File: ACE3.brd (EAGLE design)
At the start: 160 x 100 mm, 141 parts, among them IC1 7805T, IC2 74HCT04N, IC3 74HCT08N, Q1 2N3904, Q3 BC237, T1 2N2369, X1 6.556MHz

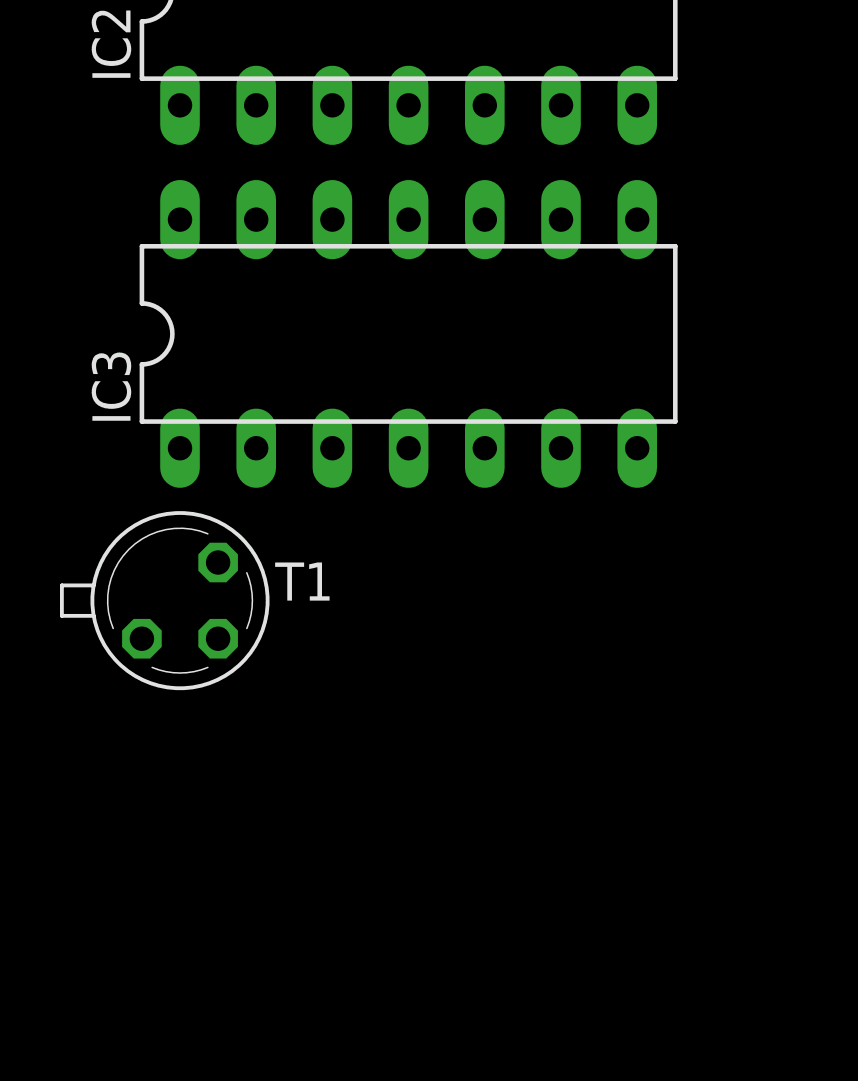
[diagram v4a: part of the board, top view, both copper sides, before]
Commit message: Make sure is correct this time. OR not AnD where needed.
Signed-off-by: John Bradley <flypie@rocketmail.com>
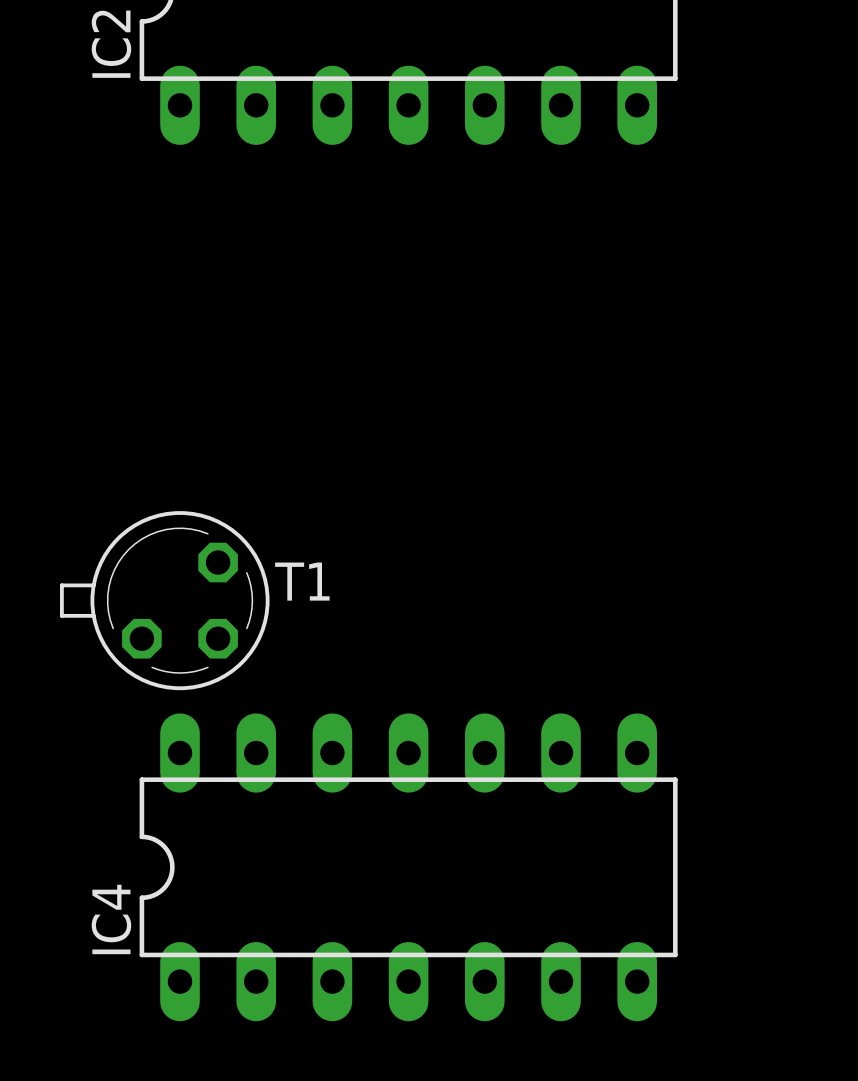
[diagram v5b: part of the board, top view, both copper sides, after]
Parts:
- removed IC3: 74HCT08N, 74xx-eu:DIL14
- added IC4: 74LS32N, 74xx-eu:DIL14
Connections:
- net ADDRESS12: now also IC4.1; no longer IC3.4
- net GND: now also IC4.7; no longer IC3.7
- net N$2: now also IC4.3; no longer IC3.3
- net N$30: now also IC4.4; no longer IC3.1
- net N$6: now also IC4.2, IC4.5; no longer IC3.2, IC3.5
- net N$7: now also IC4.6; no longer IC3.6
- net VCC: now also IC4.14; no longer IC3.14
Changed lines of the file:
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@@
 <attribute name="VALUE" x="-154.051" y="-6.985" size="1.27" layer="27" ratio="10"/>
-</element>
-<element name="IC3" library="74xx-eu" library_urn="urn:adsk.eagle:library:85" package="DIL14" package3d_urn="urn:adsk.eagle:package:16407/2" value="74HCT08N" x="-147.32" y="-17.78" smashed="yes">
-<attribute name="NAME" x="-156.591" y="-20.828" size="1.27" layer="25" ratio="10" rot="R90"/>
-<attribute name="VALUE" x="-154.051" y="-18.415" size="1.27" layer="27" ratio="10"/>
 </element>
 <element name="T1" library="transistor" library_urn="urn:adsk.eagle:library:402" package="TO18" package3d_urn="urn:adsk.eagle:package:28526/2" value="2N2369" x="-154.94" y="-26.67" smashed="yes">
 <attribute name="NAME" x="-151.765" y="-26.67" size="1.27" layer="25" ratio="10"/>
 <attribute name="VALUE" x="-151.765" y="-28.575" size="1.27" layer="27" ratio="10"/>
+</element>
+<element name="IC4" library="74xx-eu" library_urn="urn:adsk.eagle:library:85" package="DIL14" package3d_urn="urn:adsk.eagle:package:16407/2" value="74LS32N" x="-147.32" y="-35.56" smashed="yes">
+<attribute name="NAME" x="-156.591" y="-38.608" size="1.27" layer="25" ratio="10" rot="R90"/>
+<attribute name="VALUE" x="-154.051" y="-36.195" size="1.27" layer="27" ratio="10"/>
 </element>
 </elements>
@@
 <contactref element="Z1-2" pad="27"/>
 <contactref element="IC2" pad="14"/>
-<contactref element="IC3" pad="14"/>
-<wire x1="-154.94" y1="-2.54" x2="-154.94" y2="-13.97" width="0" layer="19" extent="1-1"/>
+<contactref element="IC4" pad="14"/>
+<wire x1="-154.94" y1="-2.54" x2="-154.94" y2="-31.75" width="0" layer="19" extent="1-1"/>
 <wire x1="-101.6" y1="2.54" x2="-154.94" y2="-2.54" width="0" layer="19" extent="1-1"/>
 <wire x1="-86.36" y1="2.54" x2="-101.6" y2="2.54" width="0" layer="19" extent="1-1"/>
@@
 <contactref element="Z5-6" pad="19"/>
 <contactref element="IC2" pad="7"/>
-<contactref element="IC3" pad="7"/>
 <contactref element="T1" pad="1"/>
-<wire x1="-139.7" y1="-21.59" x2="-156.21" y2="-27.94" width="0" layer="19" extent="1-1"/>
-<wire x1="-139.7" y1="-10.16" x2="-139.7" y2="-21.59" width="0" layer="19" extent="1-1"/>
+<contactref element="IC4" pad="7"/>
+<wire x1="-139.7" y1="-39.37" x2="-156.21" y2="-27.94" width="0" layer="19" extent="1-1"/>
+<wire x1="-139.7" y1="-10.16" x2="-156.21" y2="-27.94" width="0" layer="19" extent="1-1"/>
 <wire x1="-99.06" y1="17.78" x2="-139.7" y2="-10.16" width="0" layer="19" extent="1-1"/>
 <wire x1="-92.71" y1="33.02" x2="-99.06" y2="17.78" width="0" layer="19" extent="1-1"/>
@@
 <contactref element="Z3-4" pad="2"/>
 <contactref element="Z52" pad="2"/>
-<contactref element="IC3" pad="4"/>
+<contactref element="IC4" pad="1"/>
 <contactref element="IC2" pad="1"/>
-<wire x1="-154.94" y1="-10.16" x2="-147.32" y2="-21.59" width="0" layer="19" extent="1-1"/>
+<wire x1="-154.94" y1="-10.16" x2="-154.94" y2="-39.37" width="0" layer="19" extent="1-1"/>
 <wire x1="-124.46" y1="2.54" x2="-154.94" y2="-10.16" width="0" layer="19" extent="1-1"/>
 <wire x1="-123.19" y1="33.02" x2="-124.46" y2="2.54" width="0" layer="19" extent="1-1"/>
@@
 <contactref element="R26" pad="1"/>
 <contactref element="Z26" pad="2"/>
-<contactref element="IC3" pad="3"/>
-<wire x1="-88.9" y1="128.27" x2="-149.86" y2="-21.59" width="0" layer="19" extent="1-1"/>
+<contactref element="IC4" pad="3"/>
+<wire x1="-88.9" y1="128.27" x2="-149.86" y2="-39.37" width="0" layer="19" extent="1-1"/>
 <wire x1="-114.3" y1="171.45" x2="-88.9" y2="128.27" width="0" layer="19" extent="1-1"/>
 </signal>
@@
 <wire x1="-55.88" y1="67.31" x2="-114.3" y2="113.03" width="0" layer="19" extent="1-1"/>
 </signal>
-<signal name="N$30">
-<contactref element="IC3" pad="1"/>
-<contactref element="IC2" pad="2"/>
-<wire x1="-152.4" y1="-10.16" x2="-154.94" y2="-21.59" width="0" layer="19" extent="1-1"/>
-</signal>
 <signal name="N$1">
 <contactref element="Z50" pad="4"/>
@@
 </signal>
 <signal name="N$6">
-<contactref element="IC3" pad="5"/>
 <contactref element="Z29" pad="14"/>
-<contactref element="IC3" pad="2"/>
-<wire x1="-144.78" y1="-21.59" x2="-152.4" y2="-21.59" width="0" layer="19" extent="1-1"/>
-<wire x1="-142.24" y1="113.03" x2="-144.78" y2="-21.59" width="0" layer="19" extent="1-1"/>
+<contactref element="IC4" pad="2"/>
+<contactref element="IC4" pad="5"/>
+<wire x1="-144.78" y1="-39.37" x2="-152.4" y2="-39.37" width="0" layer="19" extent="1-1"/>
+<wire x1="-142.24" y1="113.03" x2="-144.78" y2="-39.37" width="0" layer="19" extent="1-1"/>
 </signal>
 <signal name="N$7">
-<contactref element="IC3" pad="6"/>
 <contactref element="Z50" pad="1"/>
-<wire x1="-132.08" y1="128.27" x2="-142.24" y2="-21.59" width="0" layer="19" extent="1-1"/>
+<contactref element="IC4" pad="6"/>
+<wire x1="-132.08" y1="128.27" x2="-142.24" y2="-39.37" width="0" layer="19" extent="1-1"/>
 </signal>
 <signal name="N$23">
@@
 <wire x1="-144.78" y1="124.46" x2="-132.08" y2="105.41" width="0" layer="19" extent="1-1"/>
 </signal>
+<signal name="N$30">
+<contactref element="IC4" pad="4"/>
+<contactref element="IC2" pad="2"/>
+<wire x1="-152.4" y1="-10.16" x2="-147.32" y2="-39.37" width="0" layer="19" extent="1-1"/>
+</signal>
 </signals>

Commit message: Update parts to either LS or HCT if no LS available,  Revert to orginal numbering scheme.
Signed-off-by: John Bradley <flypie@rocketmail.com>
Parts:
- removed JP1, JP2, JP4: 1503_02, con-lumberg:1503_02
- removed JP3: RC-5231, con-lumberg:RC-5231
- added AUDIO-IN, AUDIO-OUT, POWER-9V-DC-IN: 1503_04, con-lumberg:1503_04
- added VIDEO-OUT: WBTOR1, con-lumberg:WBTOR1
- Z14: value 74LS367D -> 74HCT367N; device 74xx-eu:SO16 -> 74xx-eu:DIL16
- Z15, Z16, Z17, Z18: value 74367N -> 74HCT367N
- moved Z15 255.0 mm to (-176.5, -95.2)
- moved Z18 253.0 mm to (-176.5, -129.5)
- moved Z16 251.8 mm to (-176.5, -106.7)
- moved Z17 251.1 mm to (-176.5, -118.1)
- moved Z14 230.9 mm to (-176.5, -83.8)
- renumbered Z28 to Z12, Z29 to Z13
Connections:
- net GND: now also AUDIO-IN.3, AUDIO-OUT.3, POWER-9V-DC-IN.3, VIDEO-OUT.S; no longer JP1.2, JP2.2, JP3.S, JP4.2
- net N$12: now also AUDIO-IN.1, AUDIO-IN.2; no longer JP4.1, JP4.3
- net N$29: no longer Z14.1
- net N$43: now also AUDIO-OUT.1, AUDIO-OUT.2; no longer JP1.1, JP1.3
- net N$65: now also POWER-9V-DC-IN.1, POWER-9V-DC-IN.2; no longer JP2.1, JP2.3
- net VIDEO: now also VIDEO-OUT.T; no longer JP3.T
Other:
- board size 160 x 100 mm -> 160 x 209.2 mm

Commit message: Sent test of ACE2NOKB for PCB manufacture as risk reduction execise to show schematic works.
Signed-off-by: John Bradley <flypie@rocketmail.com>
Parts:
- removed POWER-9V-DC-IN: 1503_04, con-lumberg:1503_04
- removed VIDEO-OUT: WBTOR1, con-lumberg:WBTOR1
- added COMPOSITE-OUT, POWER-IN-9V-DC: (no value), con-amp-mt:L02P
- AUDIO-IN, AUDIO-OUT: value 1503_04 -> (none); device con-lumberg:1503_04 -> con-amp-mt:L02P
- moved AUDIO-OUT 350.1 mm to (123.2, 120.7)
- moved Z14 344.8 mm to (129.5, 74.9)
- moved Z15 344.8 mm to (129.5, 63.5)
- moved Z16 344.8 mm to (129.5, 52.1)
- moved Z17 344.8 mm to (129.5, 40.6)
- moved Z18 344.8 mm to (129.5, 29.2)
- moved AUDIO-IN 335.8 mm to (135.9, 73.7)
- moved RN2 260.7 mm to (108.0, 8.89)
- moved S17 244.2 mm to (94.0, 88.9)
- moved S31 244.2 mm to (94.0, 100.3)
- moved S13 244.2 mm to (134.6, 88.9)
- moved S27 244.2 mm to (134.6, 100.3)
- moved S14 244.2 mm to (124.5, 88.9)
- moved S15 244.2 mm to (114.3, 88.9)
- moved S16 244.2 mm to (104.1, 88.9)
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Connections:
- new net N$83: IC2.13, Z26.8
- net /RD: now also Z24.6; no longer Z26.10
- net /WR: now also Z24.3; no longer Z25.9
- net ADDRESS11: now also Z25.9; no longer Z24.6
- net CSB4KV: now also IC2.12; no longer Z24.1
- net CST4KV: now also Z25.10, Z26.10; no longer Z24.3, Z24.4
- net GND: now also AUDIO-IN.2, AUDIO-OUT.2, COMPOSITE-OUT.2, POWER-IN-9V-DC.2; no longer AUDIO-IN.3, AUDIO-OUT.3, POWER-9V-DC-IN.3, VIDEO-OUT.S
- net N$12: no longer AUDIO-IN.2
- net N$29: now also IC2.6; no longer IC2.5, Z26.8
- net N$31: now also Z24.2, Z24.5; no longer Z25.8, Z26.9
- net N$35: now also Z24.1; no longer Z25.10
- net N$39: now also IC2.5, Z24.4; no longer IC2.6
- net N$43: no longer AUDIO-OUT.2
- net N$65: now also POWER-IN-9V-DC.1; no longer POWER-9V-DC-IN.1, POWER-9V-DC-IN.2
- net N$86: now also Z25.8, Z26.9; no longer Z24.2, Z24.5
- net VIDEO: now also COMPOSITE-OUT.1; no longer VIDEO-OUT.T
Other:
- board size 160 x 209.2 mm -> 140.9 x 117.8 mm

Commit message: tidy
Signed-off-by: John Bradley <flypie@rocketmail.com>
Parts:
- removed Z52: CY62256, memory-idt:DIL28-6
- D1, D10, D11, D2, D3, D4, D5, D6, D7, D8, D9: value 1N4148DO35-7 -> 1N4148DO35; device diode:DO35-7 -> diode:D-2.5
- Z1-2: value 2764 -> (none)
- Z3-4: value CY62256 -> AS6C1008-55PCN; device memory-idt:DIL28-6 -> AS6C1008-55PCN:DIP254P1524X393-32
- moved D10 295.0 mm to (-156.2, -130.8)
- moved D5 293.2 mm to (-156.2, -99.1)
- moved D9 292.0 mm to (-156.2, -124.5)
- moved D8 290.1 mm to (-156.2, -118.1)
- moved D6 284.9 mm to (-156.2, -105.4)
- moved D7 277.5 mm to (-156.2, -111.8)
- moved D4 245.1 mm to (-156.2, -92.7)
- moved D3 239.5 mm to (-156.2, -86.4)
- moved D2 228.8 mm to (-156.2, -73.7)
- moved D1 225.8 mm to (-156.2, -67.3)
- moved D11 223.4 mm to (-156.2, -61.0)
- moved Z1-2 212.3 mm to (-137.2, -48.3)
- moved Z3-4 188.6 mm to (-160.0, -125.7)
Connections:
- removed net CY1: Z22.8, Z52.20
- removed net CY62256: Z3-4.20, Z50.6
- new net N$72: Z50.6, Z50.9
- new net N$87: Z19.12, Z19.13, Z3-4.22, Z50.8
- new net N$88: Z19.11, Z3-4.30
- net /RD: now also Z3-4.24; no longer Z3-4.22, Z52.22
- net /WR: now also Z3-4.29; no longer Z3-4.27, Z52.27
- net ADDRESS0: now also Z3-4.12; no longer Z3-4.10, Z52.10
- net ADDRESS1: now also Z3-4.11; no longer Z3-4.9, Z52.9
- net ADDRESS10: now also Z3-4.23; no longer Z3-4.21, Z52.21
- net ADDRESS11: now also Z3-4.25; no longer Z3-4.23, Z52.23
- net ADDRESS12: now also Z3-4.4; no longer Z3-4.2, Z52.2
- net ADDRESS13: now also Z1-2.26, Z3-4.28; no longer Z3-4.26, Z52.26
- net ADDRESS14: now also Z1-2.27, Z3-4.3; no longer Z3-4.1, Z52.1
- net ADDRESS15: now also Z3-4.31
- net ADDRESS2: now also Z3-4.10; no longer Z3-4.8, Z52.8
- net ADDRESS3: now also Z3-4.9; no longer Z3-4.7, Z52.7
- net ADDRESS4: now also Z3-4.8; no longer Z3-4.6, Z52.6
- net ADDRESS5: now also Z3-4.7; no longer Z3-4.5, Z52.5
- net ADDRESS6: now also Z3-4.6; no longer Z3-4.4, Z52.4
- net ADDRESS7: now also Z3-4.5; no longer Z3-4.3, Z52.3
- net ADDRESS8: now also Z3-4.27; no longer Z3-4.25, Z52.25
- net ADDRESS9: now also Z3-4.26; no longer Z3-4.24, Z52.24
- net DATA0: now also Z3-4.13; no longer Z3-4.11, Z52.11
- net DATA1: now also Z3-4.14; no longer Z3-4.12, Z52.12
- net DATA2: now also Z3-4.15; no longer Z3-4.13, Z52.13
- net DATA3: now also Z3-4.17; no longer Z3-4.15, Z52.15
- net DATA4: now also Z3-4.18; no longer Z3-4.16, Z52.16
- net DATA5: now also Z3-4.19; no longer Z3-4.17, Z52.17
- net DATA6: now also Z3-4.20; no longer Z3-4.18, Z52.18
- net DATA7: now also Z3-4.21; no longer Z3-4.19, Z52.19
- net GND: now also Z3-4.2; no longer Z3-4.14, Z52.14
- net N$23: now also Z50.10; no longer Z22.9
- net N$25: now also Z50.12; no longer Z22.10
- net N$28: now also Z50.13; no longer Z22.11
- net VCC: no longer Z1-2.1, Z1-2.27, Z3-4.28, Z52.28
